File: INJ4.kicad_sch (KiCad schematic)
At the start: 6 parts, among them U1 VNLD5160TR-E, U2 VNLD5160TR-E

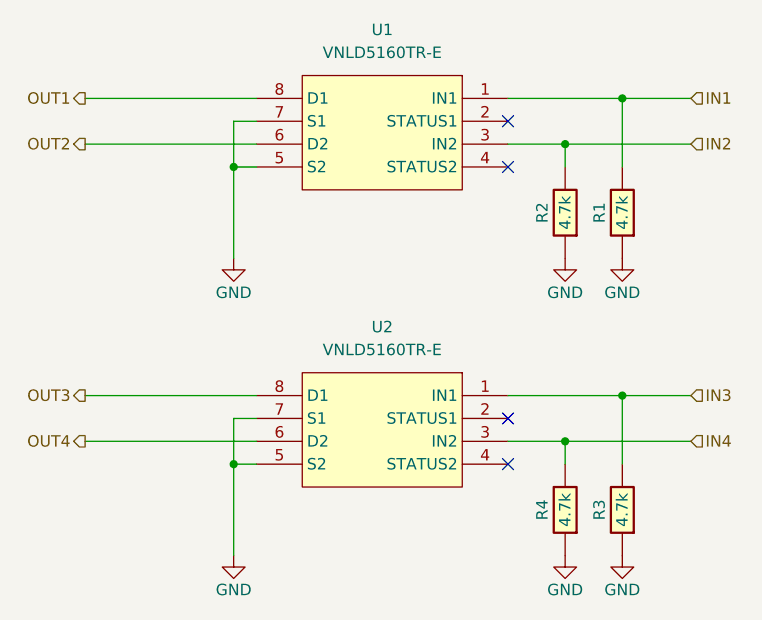
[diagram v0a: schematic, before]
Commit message: add submodules for ign and inj + flyback protected output
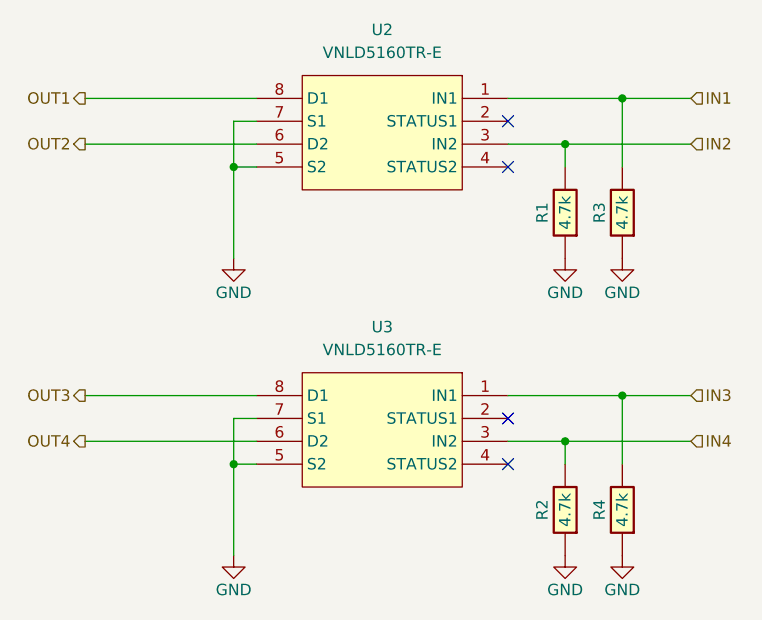
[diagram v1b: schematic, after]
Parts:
- R1: renamed from R2; footprint hellen-one-common:R0603 -> footprints:R0603
- R2: renamed from R4; footprint hellen-one-common:R0603 -> footprints:R0603
- R3: renamed from R1; footprint hellen-one-common:R0603 -> footprints:R0603
- R4: renamed from R3; footprint hellen-one-common:R0603 -> footprints:R0603
- renumbered U1 to U2, U2 to U3
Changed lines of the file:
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@@
 		(on_board yes)
 		(dnp no)
-		(property "Reference" "#PWR?"
+		(property "Reference" "#PWR5"
 			(at 165.1 101.6 0)
 			(effects
@@
 			(project "EP91Starlet"
 				(path "/10fbc709-889c-4565-8161-129ca9f0b73f/be1c43af-891a-42a9-806b-74d195d7f62c"
-					(reference "#PWR?")
+					(reference "#PWR5")
 					(unit 1)
 				)
@@
 		(on_board yes)
 		(dnp no)
-		(property "Reference" "R1"
+		(property "Reference" "R3"
 			(at 162.56 90.17 0)
 			(effects
@@
 			)
 		)
-		(property "Footprint" "hellen-one-common:R0603"
+		(property "Footprint" "footprints:R0603"
 			(at 168.91 91.44 0)
 			(effects
@@
 			(project "EP91Starlet"
 				(path "/10fbc709-889c-4565-8161-129ca9f0b73f/be1c43af-891a-42a9-806b-74d195d7f62c"
-					(reference "R1")
+					(reference "R3")
 					(unit 1)
 				)
@@
 		(on_board yes)
 		(dnp no)
-		(property "Reference" "U2"
+		(property "Reference" "U3"
 			(at 138.43 102.87 0)
 			(effects
@@
 			(project "EP91Starlet"
 				(path "/10fbc709-889c-4565-8161-129ca9f0b73f/be1c43af-891a-42a9-806b-74d195d7f62c"
-					(reference "U2")
+					(reference "U3")
 					(unit 1)
 				)
@@
 		(on_board yes)
 		(dnp no)
-		(property "Reference" "R2"
+		(property "Reference" "R1"
 			(at 156.21 90.17 0)
 			(effects
@@
 			)
 		)
-		(property "Footprint" "hellen-one-common:R0603"
+		(property "Footprint" "footprints:R0603"
 			(at 162.56 91.44 0)
 			(effects
@@
 			(project "EP91Starlet"
 				(path "/10fbc709-889c-4565-8161-129ca9f0b73f/be1c43af-891a-42a9-806b-74d195d7f62c"
-					(reference "R2")
+					(reference "R1")
 					(unit 1)
 				)
@@
 		(on_board yes)
 		(dnp no)
-		(property "Reference" "#PWR?"
+		(property "Reference" "#PWR4"
 			(at 158.75 134.62 0)
 			(effects
@@
 			(project "EP91Starlet"
 				(path "/10fbc709-889c-4565-8161-129ca9f0b73f/be1c43af-891a-42a9-806b-74d195d7f62c"
-					(reference "#PWR?")
+					(reference "#PWR4")
 					(unit 1)
 				)
@@
 		(on_board yes)
 		(dnp no)
-		(property "Reference" "#PWR?"
+		(property "Reference" "#PWR3"
 			(at 158.75 101.6 0)
 			(effects
@@
 			(project "EP91Starlet"
 				(path "/10fbc709-889c-4565-8161-129ca9f0b73f/be1c43af-891a-42a9-806b-74d195d7f62c"
-					(reference "#PWR?")
+					(reference "#PWR3")
 					(unit 1)
 				)
@@
 		(on_board yes)
 		(dnp no)
-		(property "Reference" "R3"
+		(property "Reference" "R4"
 			(at 162.56 123.19 0)
 			(effects
@@
 			)
 		)
-		(property "Footprint" "hellen-one-common:R0603"
+		(property "Footprint" "footprints:R0603"
 			(at 168.91 124.46 0)
 			(effects
@@
 			(project "EP91Starlet"
 				(path "/10fbc709-889c-4565-8161-129ca9f0b73f/be1c43af-891a-42a9-806b-74d195d7f62c"
-					(reference "R3")
+					(reference "R4")
 					(unit 1)
 				)
@@
 		(on_board yes)
 		(dnp no)
-		(property "Reference" "R4"
+		(property "Reference" "R2"
 			(at 156.21 123.19 0)
 			(effects
@@
 			)
 		)
-		(property "Footprint" "hellen-one-common:R0603"
+		(property "Footprint" "footprints:R0603"
 			(at 162.56 124.46 0)
 			(effects
@@
 			(project "EP91Starlet"
 				(path "/10fbc709-889c-4565-8161-129ca9f0b73f/be1c43af-891a-42a9-806b-74d195d7f62c"
-					(reference "R4")
+					(reference "R2")
 					(unit 1)
 				)
@@
 		(on_board yes)
 		(dnp no)
-		(property "Reference" "#PWR?"
+		(property "Reference" "#PWR1"
 			(at 121.92 101.6 0)
 			(effects
@@
 			(project "EP91Starlet"
 				(path "/10fbc709-889c-4565-8161-129ca9f0b73f/be1c43af-891a-42a9-806b-74d195d7f62c"
-					(reference "#PWR?")
+					(reference "#PWR1")
 					(unit 1)
 				)
@@
 		(on_board yes)
 		(dnp no)
-		(property "Reference" "#PWR?"
+		(property "Reference" "#PWR6"
 			(at 165.1 134.62 0)
 			(effects
@@
 			(project "EP91Starlet"
 				(path "/10fbc709-889c-4565-8161-129ca9f0b73f/be1c43af-891a-42a9-806b-74d195d7f62c"
-					(reference "#PWR?")
+					(reference "#PWR6")
 					(unit 1)
 				)
@@
 		(on_board yes)
 		(dnp no)
-		(property "Reference" "U1"
+		(property "Reference" "U2"
 			(at 138.43 69.85 0)
 			(effects
@@
 			(project "EP91Starlet"
 				(path "/10fbc709-889c-4565-8161-129ca9f0b73f/be1c43af-891a-42a9-806b-74d195d7f62c"
-					(reference "U1")
+					(reference "U2")
 					(unit 1)
 				)
@@
 		(on_board yes)
 		(dnp no)
-		(property "Reference" "#PWR?"
+		(property "Reference" "#PWR2"
 			(at 121.92 134.62 0)
 			(effects
@@
 			(project "EP91Starlet"
 				(path "/10fbc709-889c-4565-8161-129ca9f0b73f/be1c43af-891a-42a9-806b-74d195d7f62c"
-					(reference "#PWR?")
-					(unit 1)
-				)
+					(reference "#PWR2")
+					(unit 1)
+				)
